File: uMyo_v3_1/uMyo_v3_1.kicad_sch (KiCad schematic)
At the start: 53 parts, among them J1 Conn_01x01_Male, J2 Conn_01x01_Male, J4 Conn_01x01_Male, J5 Conn_01x01_Male, J6 Conn_01x02_Female, J7 Conn_01x02_Female, SW1 SW_Push, U1 AD8293G80ARJZ-R2, U2 nRF52810-QFxx, U3 XC6206P332MR_SOT23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

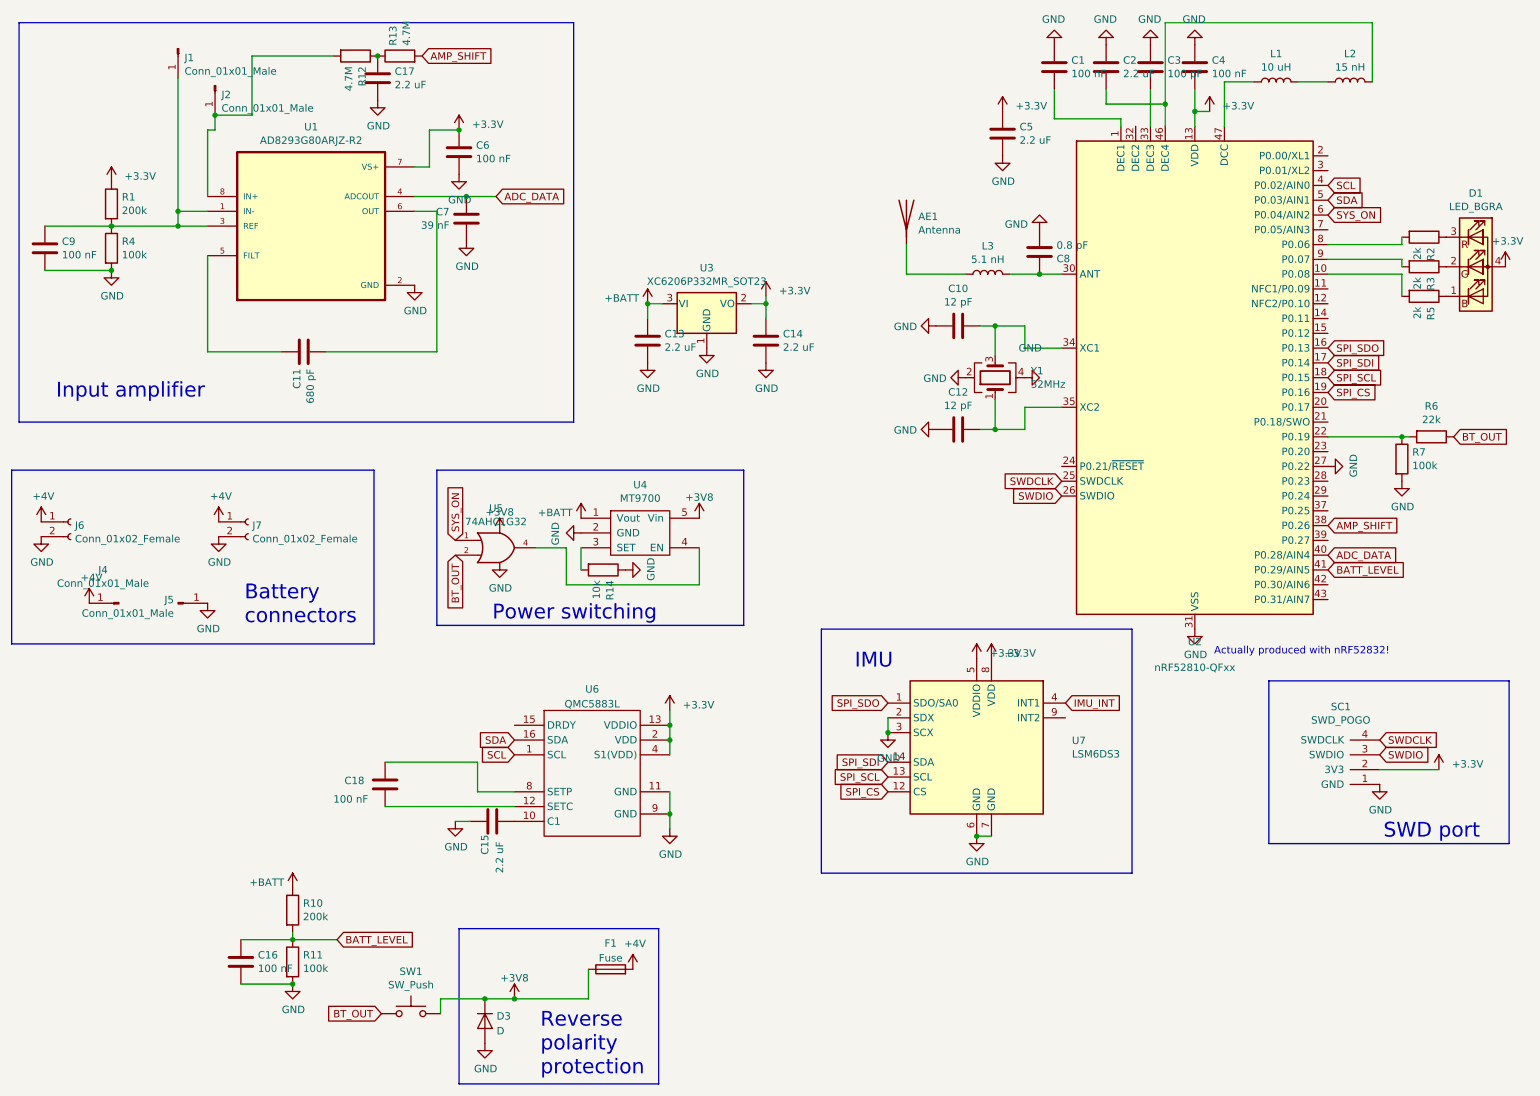
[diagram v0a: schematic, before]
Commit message: Update to the project to include available and modern parts
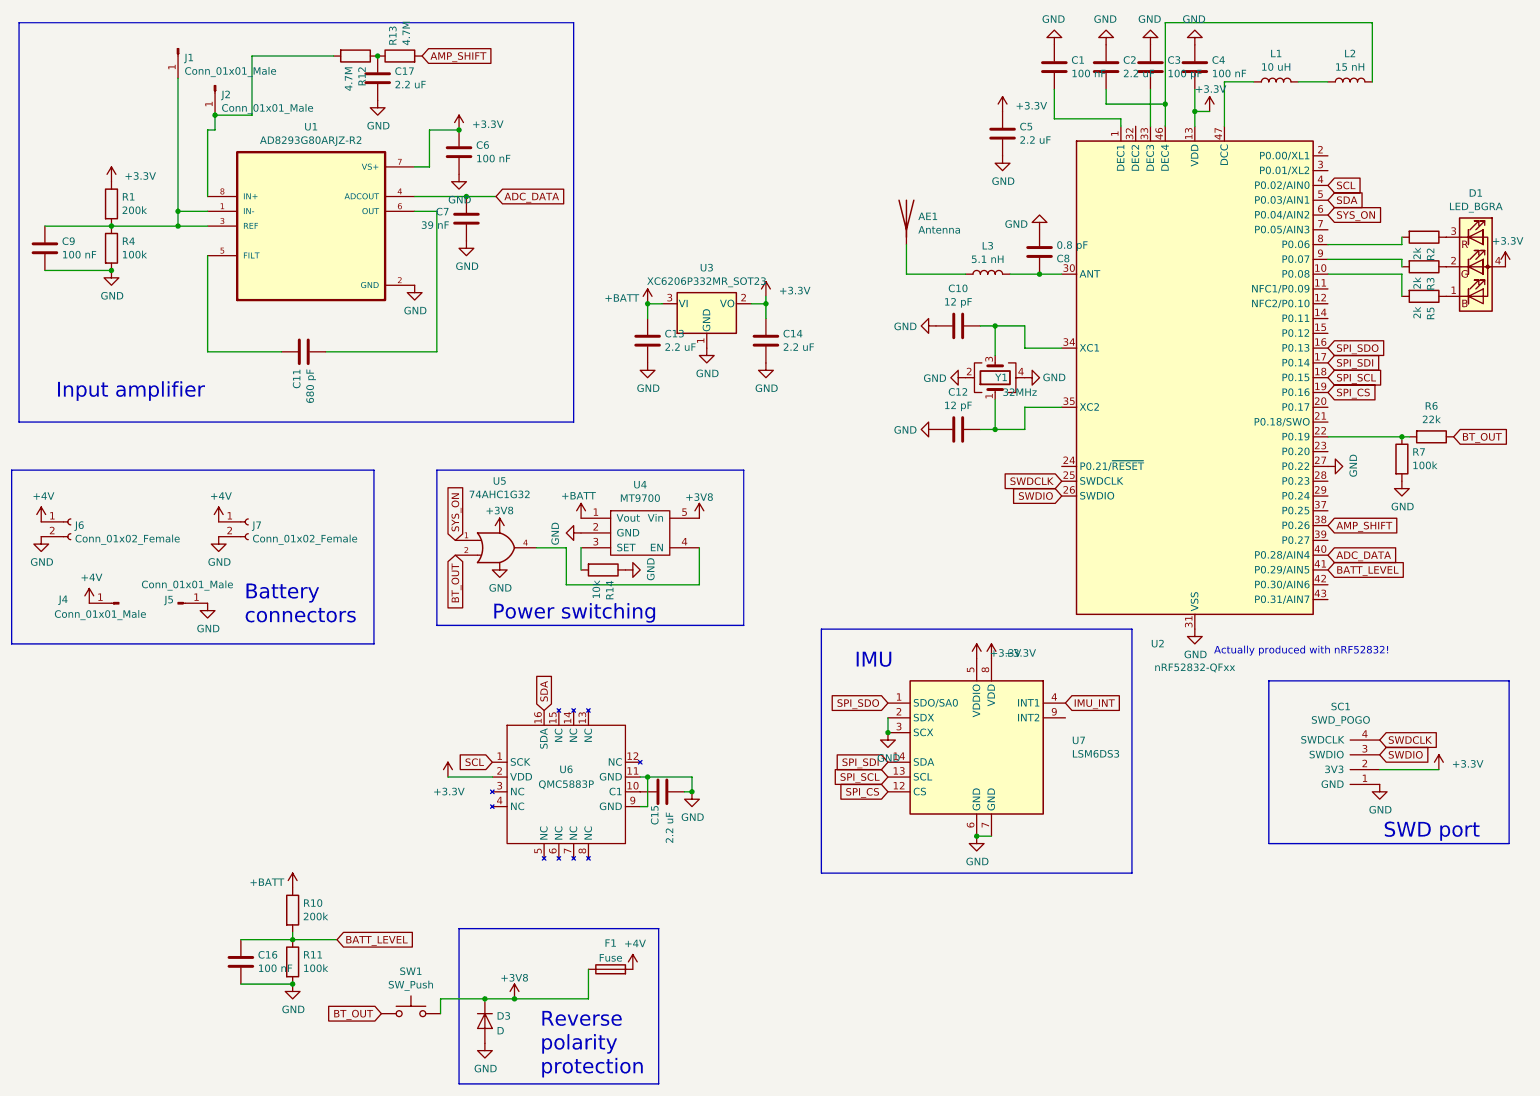
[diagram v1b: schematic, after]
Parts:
- removed C18: 100 nF, Capacitor_SMD:C_0402_1005Metric, symbol Device:C
- removed U6: QMC5883L, Package_LGA:LGA-16_3x3mm_P0.5mm, symbol ultimate_library:QMC5883L
- added U6: QMC5883P, Package_LGA:LGA-16_3x3mm_P0.5mm, symbol New_Library:QMC5883P
- U2: value nRF52810-QFxx -> nRF52832-QFxx
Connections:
- net +3V3: now also U6.2 (VDD)
- net GND: now also C15.1, U6.11 (GND), U6.9 (GND); no longer C15.2
- net SCL: now also U6.1 (SCK)
- net SDA: now also U6.16 (SDA)
- new net: C15.2, U6.10 (C1)
